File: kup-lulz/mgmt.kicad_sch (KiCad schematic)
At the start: 26 parts, among them J13 PMOD_HOST, J14 PMOD_HOST, J37 XILINX_JTAG, J38 PMOD_HOST, J39 CONN_01X03, U14 STM32L431VxIx, U15 AT24MAC402, U9 XILINX_ULTRASCALEPLUS_B676

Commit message: Continued initial layout
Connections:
- net PMODB_DQ0: now also U9.AB14 (IO_L8N_HDGC_AD4N_84); no longer U9.D13 (IO_L8N_HDGC_87)
- net PMODB_DQ1: now also U9.AA14 (IO_L8P_HDGC_AD4P_84); no longer U9.D14 (IO_L8P_HDGC_87)
- net PMODB_DQ2: now also U9.AA15 (IO_L7N_HDGC_AD5N_84); no longer U9.E12 (IO_L7N_HDGC_87)
- net PMODB_DQ3: now also U9.Y15 (IO_L7P_HDGC_AD5P_84); no longer U9.E13 (IO_L7P_HDGC_87)
- net PMODB_DQ4: now also U9.AB16 (IO_L6N_HDGC_AD6N_84); no longer U9.F13 (IO_L6N_HDGC_87)
- net PMODB_DQ5: now also U9.AB15 (IO_L6P_HDGC_AD6P_84); no longer U9.F14 (IO_L6P_HDGC_87)
- net PMODB_DQ6: now also U9.AC14 (IO_L5N_HDGC_AD7N_84); no longer U9.F12 (IO_L5N_HDGC_87)
- net PMODB_DQ7: now also U9.AC13 (IO_L5P_HDGC_AD7P_84); no longer U9.G12 (IO_L5P_HDGC_87)
- net PMOD_DQ0: now also U9.W13 (IO_L12N_AD0N_84); no longer U9.A14 (IO_L12N_AD8N_87)
- net PMOD_DQ1: now also U9.W12 (IO_L12P_AD0P_84); no longer U9.B14 (IO_L12P_AD8P_87)
- net PMOD_DQ2: now also U9.AA13 (IO_L11N_AD1N_84); no longer U9.A12 (IO_L11N_AD9N_87)
- net PMOD_DQ3: now also U9.Y13 (IO_L11P_AD1P_84); no longer U9.A13 (IO_L11P_AD9P_87)
- net PMOD_DQ4: now also U9.W15 (IO_L10N_AD2N_84); no longer U9.B12 (IO_L10N_AD10N_87)
- net PMOD_DQ5: now also U9.W14 (IO_L10P_AD2P_84); no longer U9.C12 (IO_L10P_AD10P_87)
- net PMOD_DQ6: now also U9.Y16 (IO_L9N_AD3N_84); no longer U9.C13 (IO_L9N_AD11N_87)
- net PMOD_DQ7: now also U9.W16 (IO_L9P_AD3P_84); no longer U9.C14 (IO_L9P_AD11P_87)
- net SFP0_I2C_SCL: now also U9.B14 (IO_L12P_AD8P_87); no longer U9.W12 (IO_L12P_AD0P_84)
- net SFP0_I2C_SDA: now also U9.A14 (IO_L12N_AD8N_87); no longer U9.W13 (IO_L12N_AD0N_84)
- net SFP0_MOD_ABS: now also U9.A13 (IO_L11P_AD9P_87); no longer U9.Y13 (IO_L11P_AD1P_84)
- net SFP0_RX_LOS: now also U9.A12 (IO_L11N_AD9N_87); no longer U9.AA13 (IO_L11N_AD1N_84)
- net SFP1_I2C_SCL: now also U9.C12 (IO_L10P_AD10P_87); no longer U9.W14 (IO_L10P_AD2P_84)
- net SFP1_I2C_SDA: now also U9.B12 (IO_L10N_AD10N_87); no longer U9.W15 (IO_L10N_AD2N_84)
- net SFP1_MOD_ABS: now also U9.C14 (IO_L9P_AD11P_87); no longer U9.W16 (IO_L9P_AD3P_84)
- net SFP1_RX_LOS: now also U9.C13 (IO_L9N_AD11N_87); no longer U9.Y16 (IO_L9N_AD3N_84)
- net SFP2_I2C_SCL: now also U9.D14 (IO_L8P_HDGC_87); no longer U9.AA14 (IO_L8P_HDGC_AD4P_84)
- net SFP2_I2C_SDA: now also U9.D13 (IO_L8N_HDGC_87); no longer U9.AB14 (IO_L8N_HDGC_AD4N_84)
- net SFP2_MOD_ABS: now also U9.E13 (IO_L7P_HDGC_87); no longer U9.Y15 (IO_L7P_HDGC_AD5P_84)
- net SFP2_RX_LOS: now also U9.E12 (IO_L7N_HDGC_87); no longer U9.AA15 (IO_L7N_HDGC_AD5N_84)
- net SFP3_I2C_SCL: now also U9.F14 (IO_L6P_HDGC_87); no longer U9.AB15 (IO_L6P_HDGC_AD6P_84)
- net SFP3_I2C_SDA: now also U9.F13 (IO_L6N_HDGC_87); no longer U9.AB16 (IO_L6N_HDGC_AD6N_84)
- net SFP3_MOD_ABS: now also U9.G12 (IO_L5P_HDGC_87); no longer U9.AC13 (IO_L5P_HDGC_AD7P_84)
- net SFP3_RX_LOS: now also U9.F12 (IO_L5N_HDGC_87); no longer U9.AC14 (IO_L5N_HDGC_AD7N_84)
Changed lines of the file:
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@@
     (effects (font (size 1.27 1.27)) (justify right bottom))
   )
-  (label "PMOD_DQ0" (at 36.83 62.23 180)
+  (label "PMOD_DQ0" (at 171.45 62.23 180)
     (effects (font (size 1.27 1.27)) (justify right bottom))
   )
@@
     (effects (font (size 1.27 1.27)) (justify right bottom))
   )
-  (label "PMOD_DQ6" (at 36.83 77.47 180)
+  (label "PMOD_DQ6" (at 171.45 77.47 180)
     (effects (font (size 1.27 1.27)) (justify right bottom))
   )
@@
     (effects (font (size 1.27 1.27)) (justify right bottom))
   )
-  (label "SFP2_MOD_ABS" (at 171.45 90.17 180)
+  (label "SFP2_MOD_ABS" (at 36.83 90.17 180)
     (effects (font (size 1.27 1.27)) (justify right bottom))
   )
@@
     (effects (font (size 1.27 1.27)) (justify right bottom))
   )
-  (label "SFP1_RX_LOS" (at 171.45 77.47 180)
+  (label "SFP1_RX_LOS" (at 36.83 77.47 180)
     (effects (font (size 1.27 1.27)) (justify right bottom))
   )
@@
     (effects (font (size 1.27 1.27)) (justify right bottom))
   )
-  (label "PMOD_DQ1" (at 36.83 64.77 180)
-    (effects (font (size 1.27 1.27)) (justify right bottom))
-  )
-  (label "PMODB_DQ1" (at 36.83 85.09 180)
-    (effects (font (size 1.27 1.27)) (justify right bottom))
-  )
-  (label "PMOD_DQ3" (at 36.83 69.85 180)
+  (label "PMOD_DQ1" (at 171.45 64.77 180)
+    (effects (font (size 1.27 1.27)) (justify right bottom))
+  )
+  (label "PMODB_DQ1" (at 171.45 85.09 180)
+    (effects (font (size 1.27 1.27)) (justify right bottom))
+  )
+  (label "PMOD_DQ3" (at 171.45 69.85 180)
     (effects (font (size 1.27 1.27)) (justify right bottom))
   )
@@
     (effects (font (size 1.27 1.27)) (justify right bottom))
   )
-  (label "PMODB_DQ7" (at 36.83 100.33 180)
+  (label "PMODB_DQ7" (at 171.45 100.33 180)
     (effects (font (size 1.27 1.27)) (justify right bottom))
   )
@@
     (effects (font (size 1.27 1.27)) (justify right bottom))
   )
-  (label "PMOD_DQ5" (at 36.83 74.93 180)
+  (label "PMOD_DQ5" (at 171.45 74.93 180)
     (effects (font (size 1.27 1.27)) (justify right bottom))
   )
@@
     (effects (font (size 1.27 1.27)) (justify right bottom))
   )
-  (label "SFP3_MOD_ABS" (at 171.45 100.33 180)
+  (label "SFP3_MOD_ABS" (at 36.83 100.33 180)
     (effects (font (size 1.27 1.27)) (justify right bottom))
   )
@@
     (effects (font (size 1.27 1.27)) (justify right bottom))
   )
-  (label "SFP1_MOD_ABS" (at 171.45 80.01 180)
-    (effects (font (size 1.27 1.27)) (justify right bottom))
-  )
-  (label "SFP3_RX_LOS" (at 171.45 97.79 180)
-    (effects (font (size 1.27 1.27)) (justify right bottom))
-  )
-  (label "PMODB_DQ5" (at 36.83 95.25 180)
+  (label "SFP1_MOD_ABS" (at 36.83 80.01 180)
+    (effects (font (size 1.27 1.27)) (justify right bottom))
+  )
+  (label "SFP3_RX_LOS" (at 36.83 97.79 180)
+    (effects (font (size 1.27 1.27)) (justify right bottom))
+  )
+  (label "PMODB_DQ5" (at 171.45 95.25 180)
     (effects (font (size 1.27 1.27)) (justify right bottom))
   )
@@
     (effects (font (size 1.27 1.27)) (justify right bottom))
   )
-  (label "PMODB_DQ6" (at 36.83 97.79 180)
-    (effects (font (size 1.27 1.27)) (justify right bottom))
-  )
-  (label "PMOD_DQ4" (at 36.83 72.39 180)
+  (label "PMODB_DQ6" (at 171.45 97.79 180)
+    (effects (font (size 1.27 1.27)) (justify right bottom))
+  )
+  (label "PMOD_DQ4" (at 171.45 72.39 180)
     (effects (font (size 1.27 1.27)) (justify right bottom))
   )
@@
     (effects (font (size 1.27 1.27)) (justify left bottom))
   )
-  (label "SFP2_RX_LOS" (at 171.45 87.63 180)
+  (label "SFP2_RX_LOS" (at 36.83 87.63 180)
     (effects (font (size 1.27 1.27)) (justify right bottom))
   )
@@
     (effects (font (size 1.27 1.27)) (justify right bottom))
   )
-  (label "PMODB_DQ2" (at 36.83 87.63 180)
-    (effects (font (size 1.27 1.27)) (justify right bottom))
-  )
-  (label "PMOD_DQ2" (at 36.83 67.31 180)
+  (label "PMODB_DQ2" (at 171.45 87.63 180)
+    (effects (font (size 1.27 1.27)) (justify right bottom))
+  )
+  (label "PMOD_DQ2" (at 171.45 67.31 180)
     (effects (font (size 1.27 1.27)) (justify right bottom))
   )
@@
     (effects (font (size 1.27 1.27)) (justify right bottom))
   )
-  (label "PMODB_DQ4" (at 36.83 92.71 180)
+  (label "PMODB_DQ4" (at 171.45 92.71 180)
     (effects (font (size 1.27 1.27)) (justify right bottom))
   )
@@
     (effects (font (size 1.27 1.27)) (justify left bottom))
   )
-  (label "SFP0_RX_LOS" (at 171.45 67.31 180)
+  (label "SFP0_RX_LOS" (at 36.83 67.31 180)
     (effects (font (size 1.27 1.27)) (justify right bottom))
   )
@@
     (effects (font (size 1.27 1.27)) (justify right bottom))
   )
-  (label "SFP0_MOD_ABS" (at 171.45 69.85 180)
+  (label "SFP0_MOD_ABS" (at 36.83 69.85 180)
     (effects (font (size 1.27 1.27)) (justify right bottom))
   )
@@
     (effects (font (size 1.27 1.27)) (justify right bottom))
   )
-  (label "PMODB_DQ3" (at 36.83 90.17 180)
+  (label "PMODB_DQ3" (at 171.45 90.17 180)
     (effects (font (size 1.27 1.27)) (justify right bottom))
   )
@@
     (effects (font (size 1.27 1.27)) (justify right bottom))
   )
-  (label "PMOD_DQ7" (at 36.83 80.01 180)
+  (label "PMOD_DQ7" (at 171.45 80.01 180)
     (effects (font (size 1.27 1.27)) (justify right bottom))
   )
@@
     (effects (font (size 1.27 1.27)) (justify right bottom))
   )
-  (label "PMODB_DQ0" (at 36.83 82.55 180)
+  (label "PMODB_DQ0" (at 171.45 82.55 180)
     (effects (font (size 1.27 1.27)) (justify right bottom))
   )
@@
     (effects (font (size 1.27 1.27)) (justify right))
   )
-  (hierarchical_label "SFP0_I2C_SDA" (shape bidirectional) (at 171.45 62.23 180)
-    (effects (font (size 1.27 1.27)) (justify right))
-  )
-  (hierarchical_label "SFP2_I2C_SCL" (shape output) (at 171.45 85.09 180)
+  (hierarchical_label "SFP0_I2C_SDA" (shape bidirectional) (at 36.83 62.23 180)
+    (effects (font (size 1.27 1.27)) (justify right))
+  )
+  (hierarchical_label "SFP2_I2C_SCL" (shape output) (at 36.83 85.09 180)
     (effects (font (size 1.27 1.27)) (justify right))
   )
@@
     (effects (font (size 1.27 1.27)) (justify right))
   )
-  (hierarchical_label "SFP1_I2C_SDA" (shape bidirectional) (at 171.45 72.39 180)
+  (hierarchical_label "SFP1_I2C_SDA" (shape bidirectional) (at 36.83 72.39 180)
     (effects (font (size 1.27 1.27)) (justify right))
   )
@@
     (effects (font (size 1.27 1.27)) (justify right))
   )
-  (hierarchical_label "SFP3_I2C_SDA" (shape bidirectional) (at 171.45 92.71 180)
+  (hierarchical_label "SFP3_I2C_SDA" (shape bidirectional) (at 36.83 92.71 180)
     (effects (font (size 1.27 1.27)) (justify right))
   )
@@
     (effects (font (size 1.27 1.27)) (justify right))
   )
-  (hierarchical_label "SFP0_I2C_SCL" (shape output) (at 171.45 64.77 180)
+  (hierarchical_label "SFP0_I2C_SCL" (shape output) (at 36.83 64.77 180)
     (effects (font (size 1.27 1.27)) (justify right))
   )
@@
     (effects (font (size 1.27 1.27)) (justify right))
   )
-  (hierarchical_label "SFP3_I2C_SCL" (shape output) (at 171.45 95.25 180)
+  (hierarchical_label "SFP3_I2C_SCL" (shape output) (at 36.83 95.25 180)
     (effects (font (size 1.27 1.27)) (justify right))
   )
@@
     (effects (font (size 1.27 1.27)) (justify right))
   )
-  (hierarchical_label "SFP2_I2C_SDA" (shape bidirectional) (at 171.45 82.55 180)
+  (hierarchical_label "SFP2_I2C_SDA" (shape bidirectional) (at 36.83 82.55 180)
     (effects (font (size 1.27 1.27)) (justify right))
   )
@@
     (effects (font (size 1.27 1.27)) (justify right))
   )
-  (hierarchical_label "SFP1_I2C_SCL" (shape output) (at 171.45 74.93 180)
-    (effects (font (size 1.27 1.27)) (justify right))
-  )
+  (hierarchical_label "SFP1_I2C_SCL" (shape output) (at 36.83 74.93 180)
+    (effects (font (size 1.27 1.27)) (justify right))
+  )

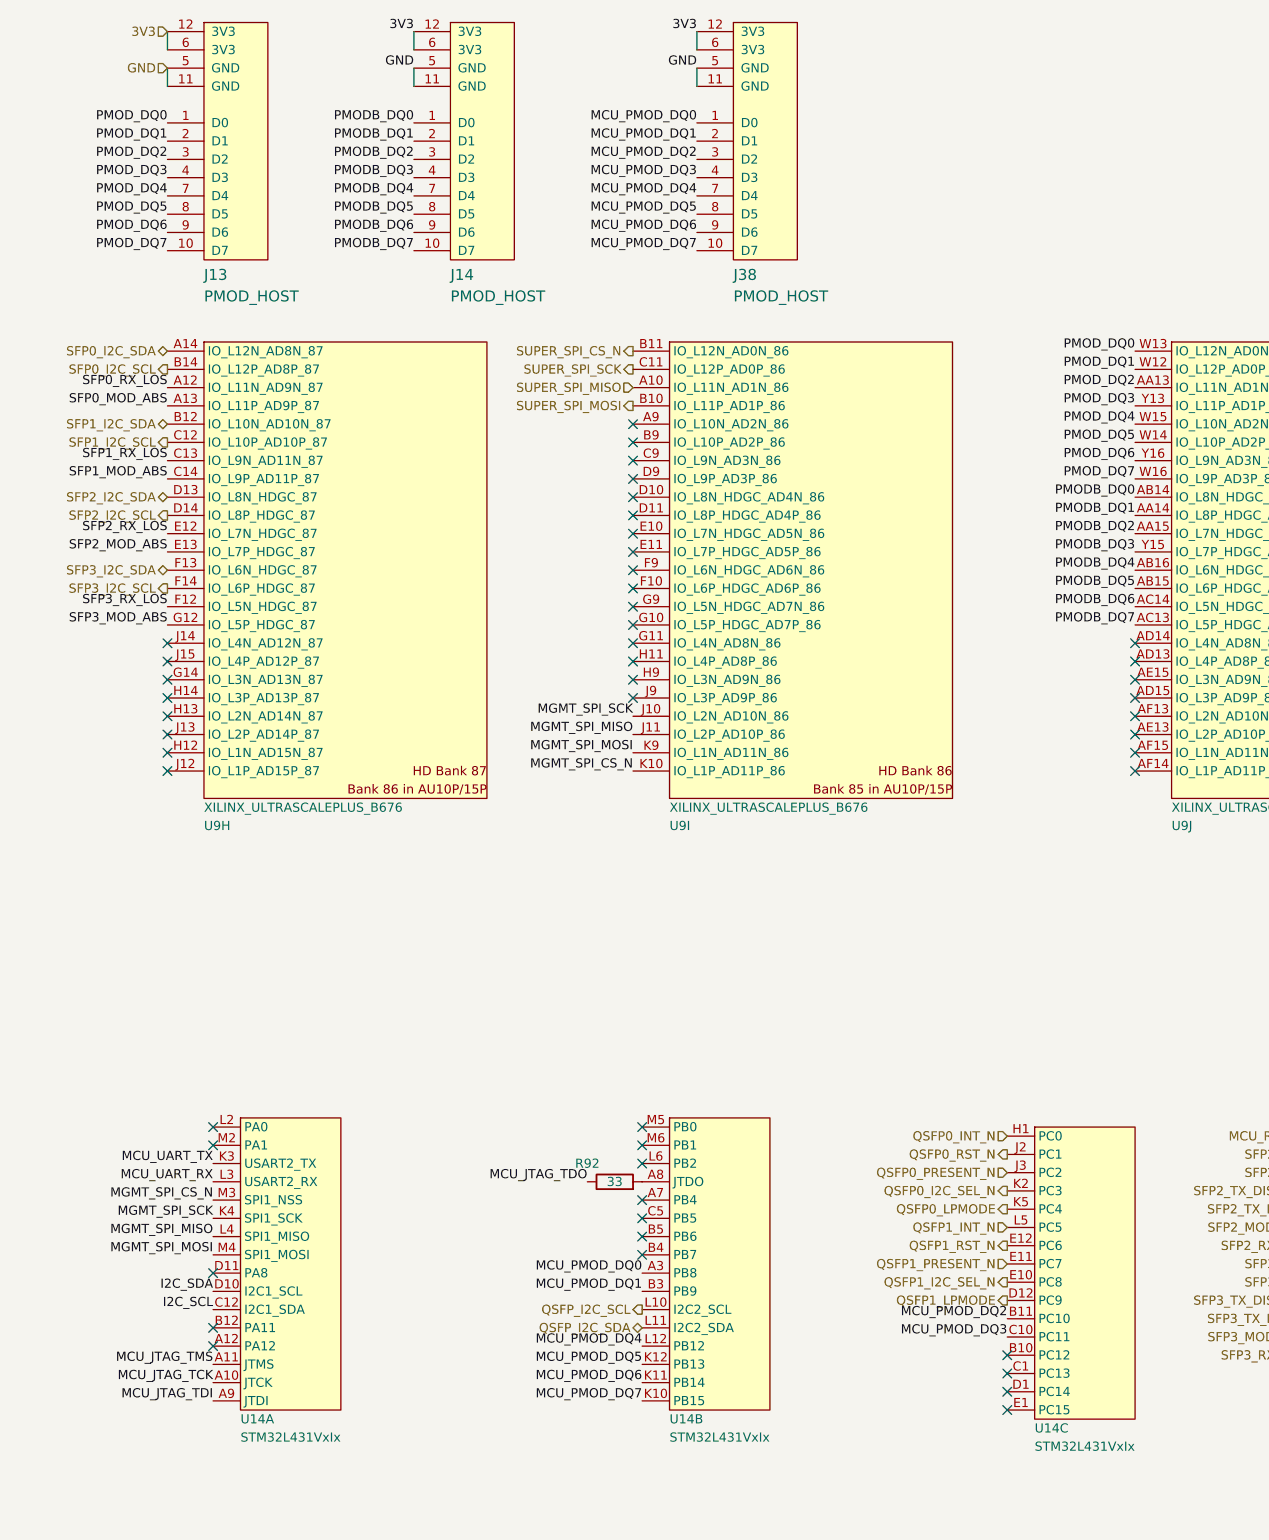
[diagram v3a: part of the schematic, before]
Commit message: Continued kup-lulz routing. Deleted one of the PMODs as there's no way it will fit.
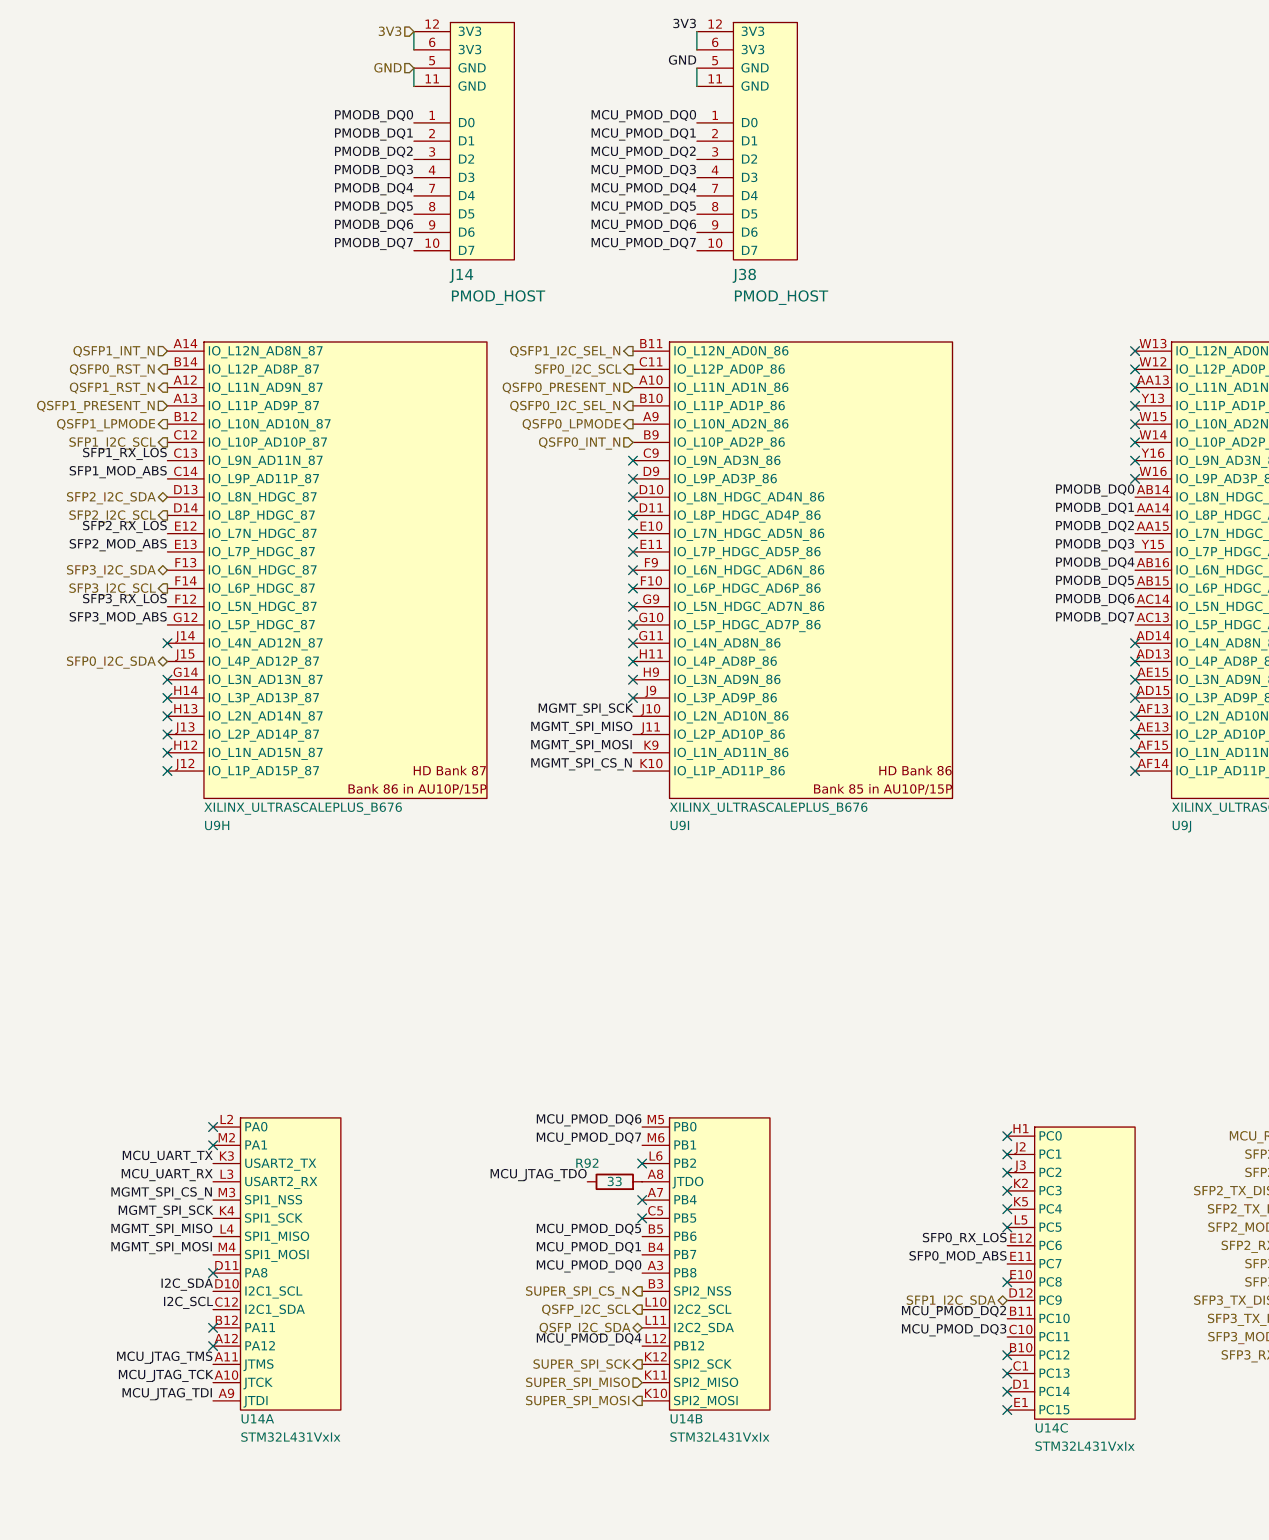
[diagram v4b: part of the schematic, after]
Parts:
- removed J13: PMOD_HOST, azonenberg_pcb:CONN_HEADER_2.54MM_2x6_RA_PMOD_HOST, symbol special-azonenberg:PMOD_HOST
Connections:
- net MCU_PMOD_DQ1: now also U14.B4 (PB7); no longer U14.B3 (PB9)
- net MCU_PMOD_DQ5: now also U14.B5 (PB6); no longer U14.K12 (PB13)
- net MCU_PMOD_DQ6: now also U14.M5 (PB0); no longer U14.K11 (PB14)
- net MCU_PMOD_DQ7: now also U14.M6 (PB1); no longer U14.K10 (PB15)
- net QSFP0_I2C_SEL_N: now also U9.B10 (IO_L11P_AD1P_86); no longer U14.K2 (PC3)
- net QSFP0_INT_N: now also U9.B9 (IO_L10P_AD2P_86); no longer U14.H1 (PC0)
- net QSFP0_LPMODE: now also U9.A9 (IO_L10N_AD2N_86); no longer U14.K5 (PC4)
- net QSFP0_PRESENT_N: now also U9.A10 (IO_L11N_AD1N_86); no longer U14.J3 (PC2)
- net QSFP0_RST_N: now also U9.B14 (IO_L12P_AD8P_87); no longer U14.J2 (PC1)
- net QSFP1_I2C_SEL_N: now also U9.B11 (IO_L12N_AD0N_86); no longer U14.E10 (PC8)
- net QSFP1_INT_N: now also U9.A14 (IO_L12N_AD8N_87); no longer U14.L5 (PC5)
- net QSFP1_LPMODE: now also U9.B12 (IO_L10N_AD10N_87); no longer U14.D12 (PC9)
- net QSFP1_PRESENT_N: now also U9.A13 (IO_L11P_AD9P_87); no longer U14.E11 (PC7)
- net QSFP1_RST_N: now also U9.A12 (IO_L11N_AD9N_87); no longer U14.E12 (PC6)
- net SFP0_I2C_SCL: now also U9.C11 (IO_L12P_AD0P_86); no longer U9.B14 (IO_L12P_AD8P_87)
- net SFP0_I2C_SDA: now also U9.J15 (IO_L4P_AD12P_87); no longer U9.A14 (IO_L12N_AD8N_87)
- net SFP0_MOD_ABS: now also U14.E11 (PC7); no longer U9.A13 (IO_L11P_AD9P_87)
- net SFP0_RX_LOS: now also U14.E12 (PC6); no longer U9.A12 (IO_L11N_AD9N_87)
- net SFP1_I2C_SDA: now also U14.D12 (PC9); no longer U9.B12 (IO_L10N_AD10N_87)
- net SUPER_SPI_CS_N: now also U14.B3 (PB9); no longer U9.B11 (IO_L12N_AD0N_86)
- net SUPER_SPI_MISO: now also U14.K11 (PB14); no longer U9.A10 (IO_L11N_AD1N_86)
- net SUPER_SPI_MOSI: now also U14.K10 (PB15); no longer U9.B10 (IO_L11P_AD1P_86)
- net SUPER_SPI_SCK: now also U14.K12 (PB13); no longer U9.C11 (IO_L12P_AD0P_86)
- net PMOD_DQ0: no longer names the net of U9.W13 (IO_L12N_AD0N_84)
- net PMOD_DQ1: no longer names the net of U9.W12 (IO_L12P_AD0P_84)
- net PMOD_DQ2: no longer names the net of U9.AA13 (IO_L11N_AD1N_84)
- net PMOD_DQ3: no longer names the net of U9.Y13 (IO_L11P_AD1P_84)
- net PMOD_DQ4: no longer names the net of U9.W15 (IO_L10N_AD2N_84)
- net PMOD_DQ5: no longer names the net of U9.W14 (IO_L10P_AD2P_84)
- net PMOD_DQ6: no longer names the net of U9.Y16 (IO_L9N_AD3N_84)
- net PMOD_DQ7: no longer names the net of U9.W16 (IO_L9P_AD3P_84)
- no-connect marks 57 -> 65
